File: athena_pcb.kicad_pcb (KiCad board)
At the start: 2 copper layers, 42.2 x 23.9 mm, 34 parts, among them J2 Conn_01x04, SW1 SW_Push, U1 NRF5340-QKAA-R7, U2 BME280, Y1 32MHz, Y2 32.768kHz

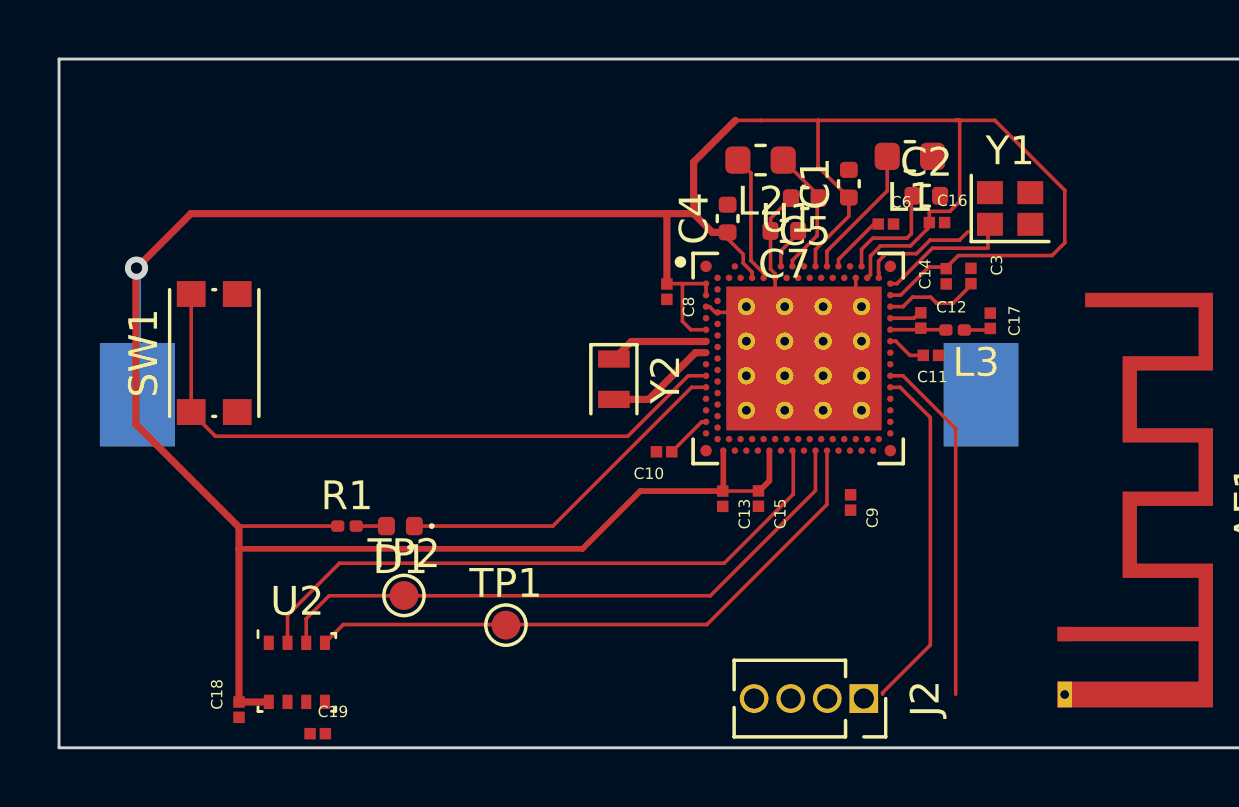
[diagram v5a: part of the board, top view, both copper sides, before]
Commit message: Added Vias acc. to PCB fab
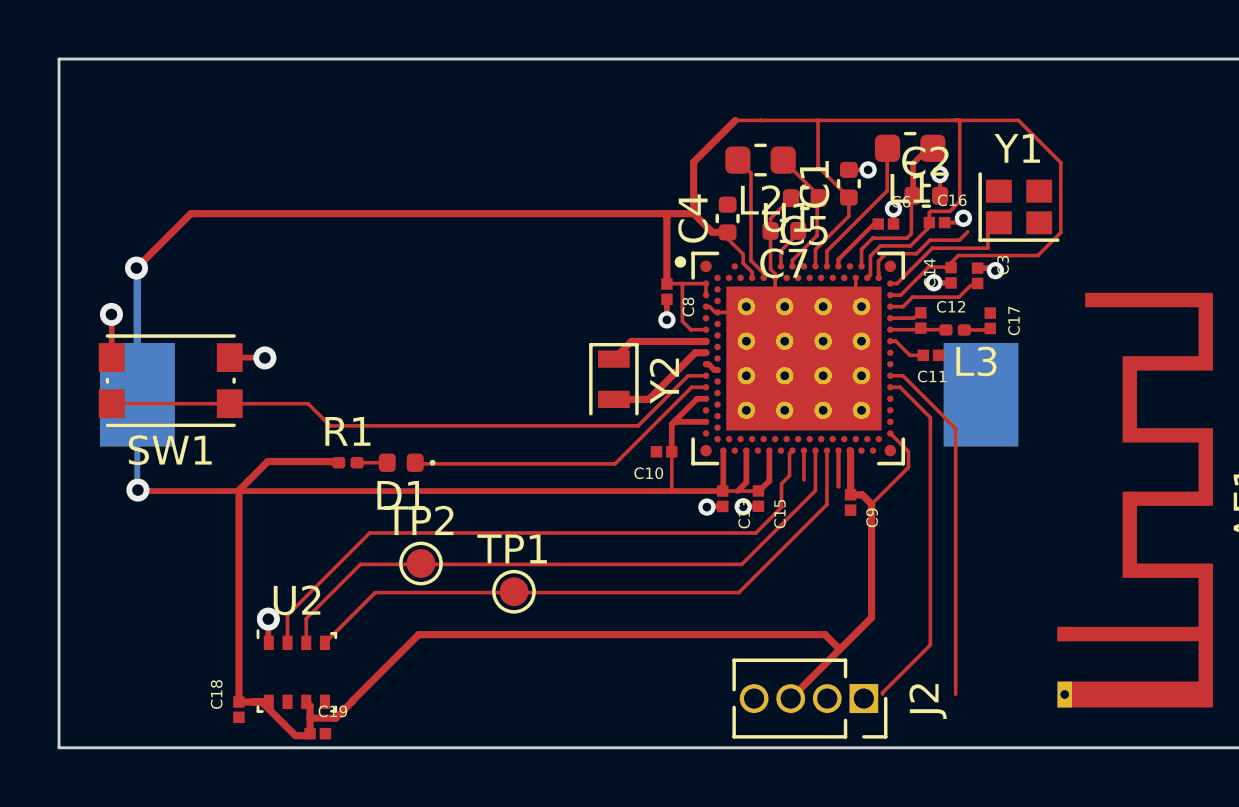
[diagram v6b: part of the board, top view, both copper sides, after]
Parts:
- moved D1 2.20 mm to (102.3, 94.4)
- moved R1 2.20 mm to (100.5, 94.4)
- moved SW1 1.79 mm to (94.3, 91.5), turned to 180 degrees
- moved TP2 1.26 mm to (103.0, 97.9)
- moved TP1 1.19 mm to (106.3, 98.8)
- moved Y1 0.31 mm to (123.8, 85.5)
- moved L1 0.28 mm to (120.0, 83.4)
- moved C3 0.23 mm to (122.4, 87.9)
- moved C14 0.17 mm to (121.4, 87.8)
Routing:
- net VDD: track 117.6 -> 158.3 mm, vias 1 -> 2
- net GND: track 12.6 -> 21.9 mm, vias 0 -> 12
- net Net-(U1A-DECR): track 6.98 -> 8.84 mm
- net /P0.02: track 23.2 -> 21.7 mm
- net unconnected-(U1D-P1.08-PadAL23): track 0.00 -> 1.25 mm
- net /P0.03: track 12.1 -> 11.2 mm

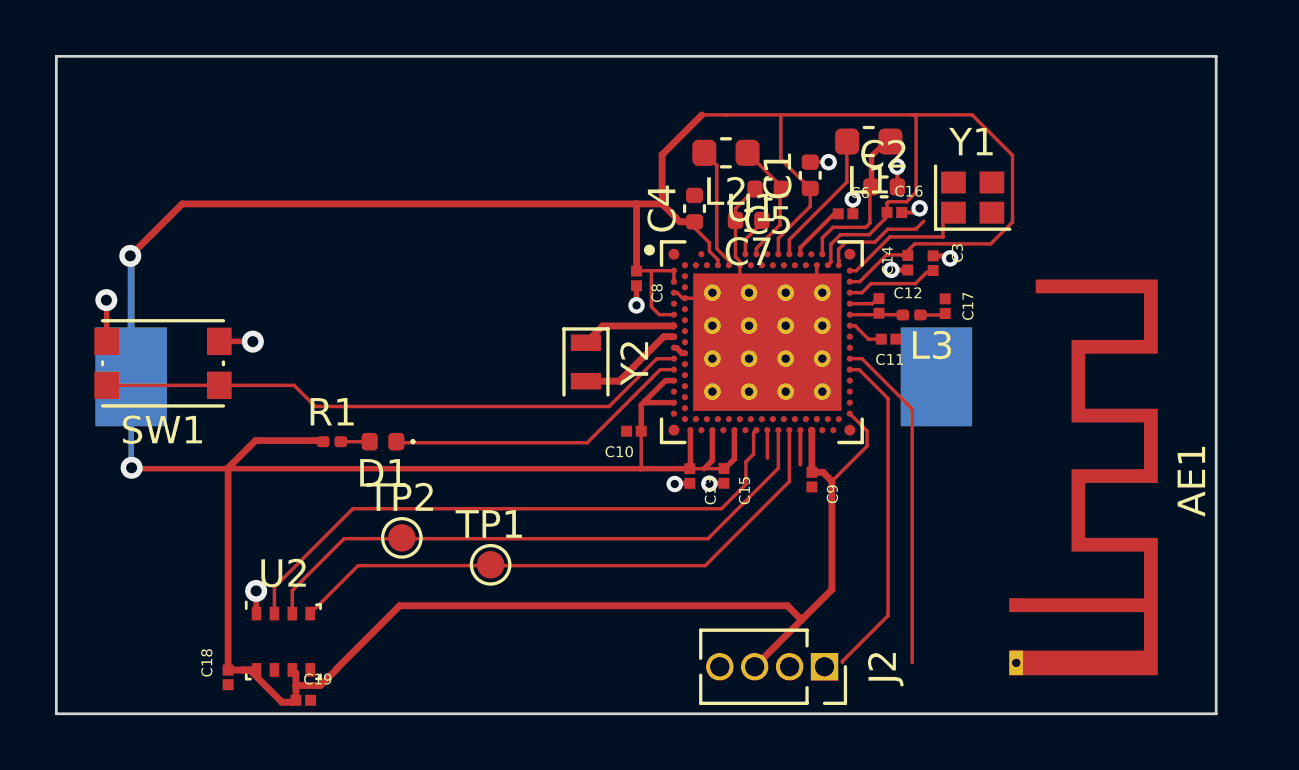
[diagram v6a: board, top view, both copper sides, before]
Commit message: Adapted PCB antenna footprint to use polygon, Workaroung for schematic symbol
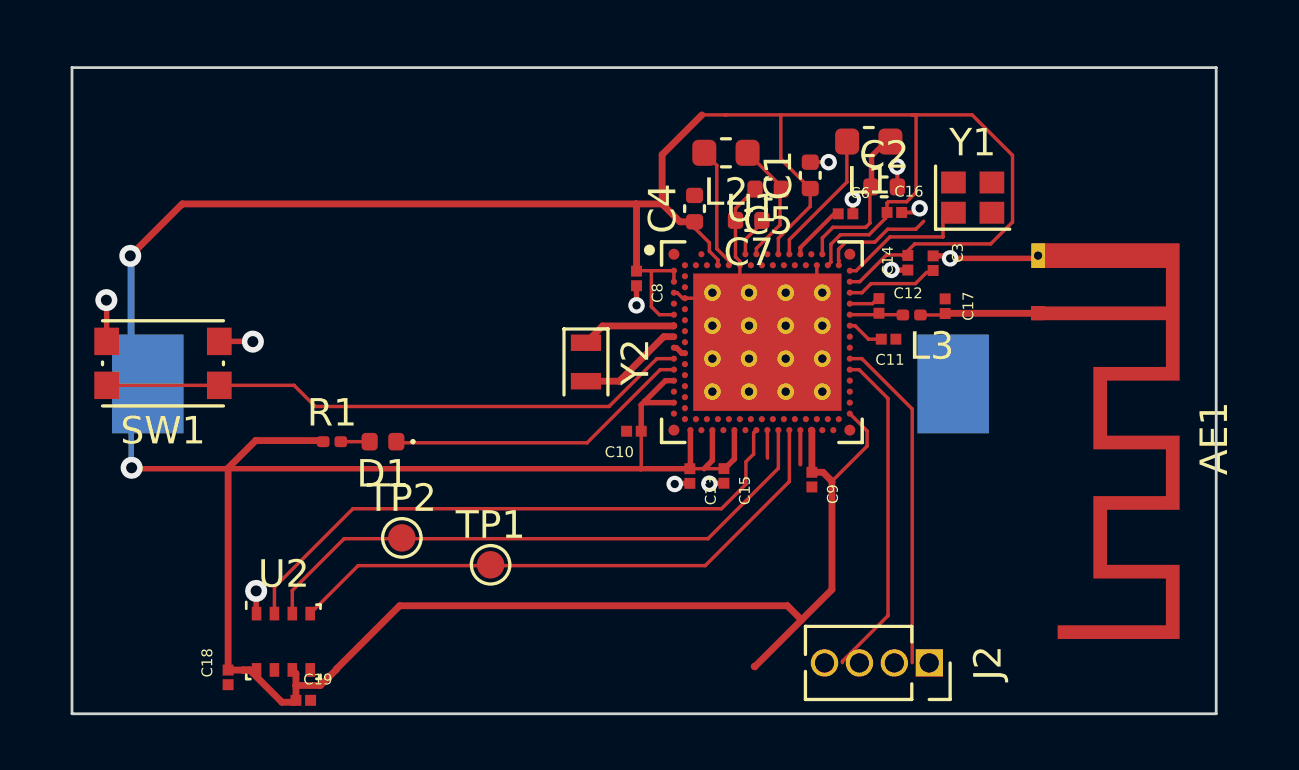
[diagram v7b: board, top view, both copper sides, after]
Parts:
- AE1: footprint RF_Antenna:Texas_SWRA117D_2.4GHz_Left -> RF_Antenna:Texas_SWRA117D_2.4GHz_Right
- moved AE1 10.6 mm to (126.2, 89.7)
- moved J2 3.81 mm to (122.2, 102.4)
- moved BT1 0.66 mm to (108.4, 92.3)
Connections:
- net Net-(U1B-ANT) renamed /ANT_LINE
- AE1 pad 1: Net-(AE1-A) -> GND
- AE1 pad 2: (no net) -> GND
- C17 pad 1: Net-(AE1-A) -> GND
- L3 pad 2: Net-(AE1-A) -> GND
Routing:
- net GND: track 21.9 -> 29.4 mm
- net Net-(AE1-A): track 0.90 -> 0.00 mm
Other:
- board size 42.2 x 23.9 mm -> 41.6 x 23.5 mm

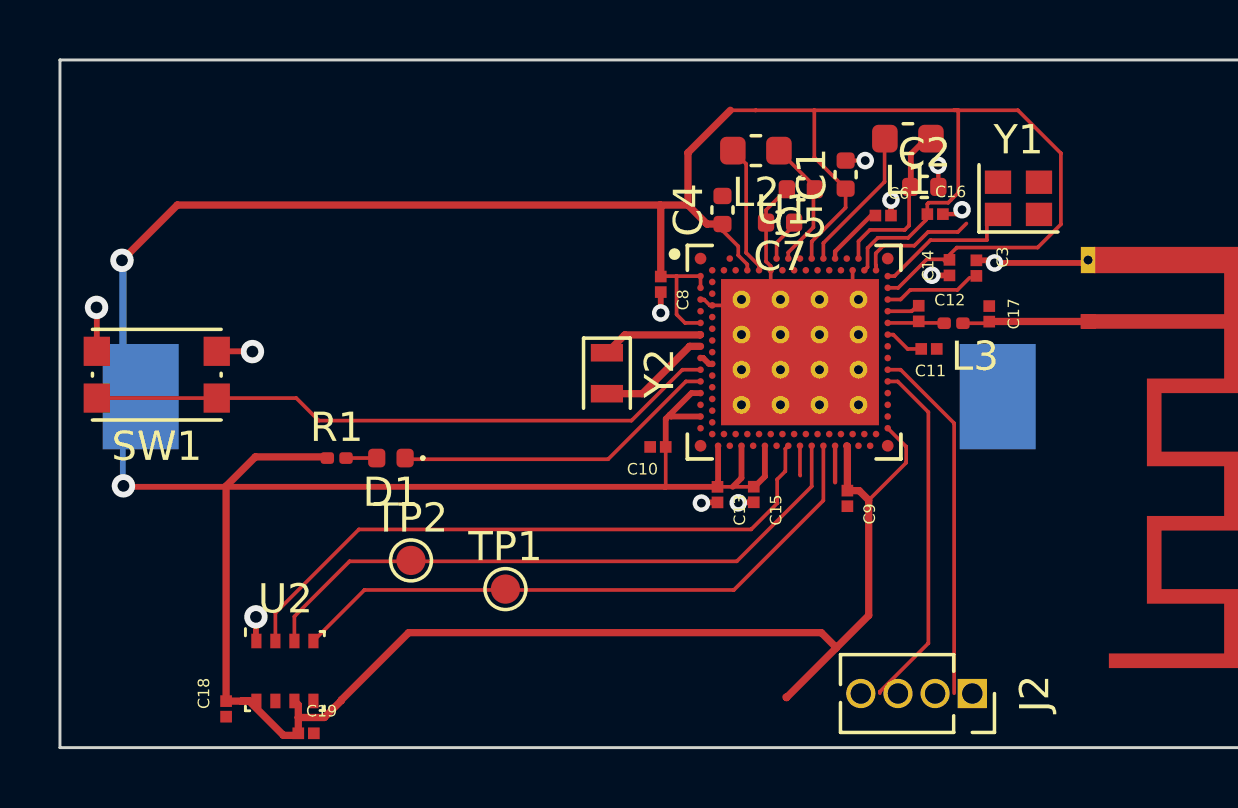
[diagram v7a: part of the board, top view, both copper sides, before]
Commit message: Added proper Y1 symbol and footprint
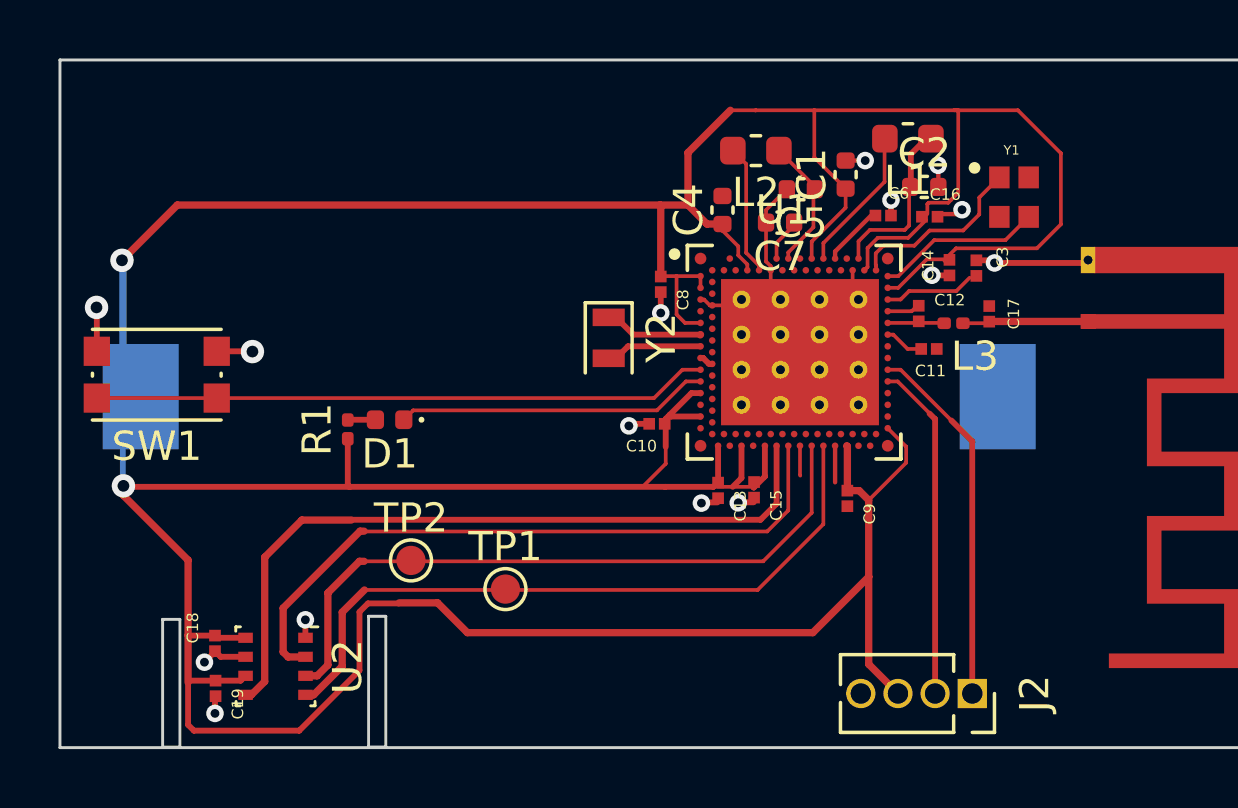
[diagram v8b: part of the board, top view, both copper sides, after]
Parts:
- Y1: footprint Crystal:Crystal_SMD_2016-4Pin_2.0x1.6mm -> XRCGB32M000F1H19R0:OSC_XRCGB32M000F1H19R0
- moved C19 3.45 mm to (96.3, 102.2), turned to -90 degrees
- moved C18 2.27 mm to (96.3, 100.7)
- moved D1 1.31 mm to (102.3, 93.0)
- moved Y2 1.21 mm to (109.8, 90.2)
- moved R1 1.05 mm to (100.9, 93.4), turned to 90 degrees
- moved C10 0.79 mm to (111.4, 93.2)
- moved U2 0.36 mm to (98.4, 101.5), turned to -90 degrees
- moved C16 0.20 mm to (120.8, 86.1)
- moved C15 0.16 mm to (114.8, 95.4)
- moved Y1 0.16 mm to (123.6, 85.4)
- moved C13 0.15 mm to (113.5, 95.5)
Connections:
- Y1 pad 1: Net-(U1B-XC1) -> Net-(U1B-XC2)
- Y1 pad 2: Net-(U1B-XC2) -> (no net)
- Y1 pad 3: (no net) -> Net-(U1B-XC1)
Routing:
- net /SDO: track 0.00 -> 25.3 mm
- net VDD: track 158.3 -> 165.1 mm
- net GND: track 29.4 -> 32.2 mm, vias 12 -> 15
- net /SCK_SCL: track 21.3 -> 23.9 mm
- net Net-(U1B-XC2): track 4.11 -> 6.22 mm
- net /SDI_SDA: track 21.8 -> 23.3 mm
- net /CSB: track 21.8 -> 23.2 mm
- net Net-(U1B-XC1): track 4.76 -> 5.66 mm
- net /SWDIO: track 12.1 -> 11.5 mm
- net /P0.02: track 21.7 -> 21.0 mm
- net Net-(U1C-P0.01/XL2): track 3.87 -> 3.31 mm
- net /P0.03: track 11.2 -> 10.7 mm
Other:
- outline, holes or cut-outs redrawn
